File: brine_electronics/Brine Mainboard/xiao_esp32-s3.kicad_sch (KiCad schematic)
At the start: 3 parts, among them U1 XIAO-ESP32-S3-SMD

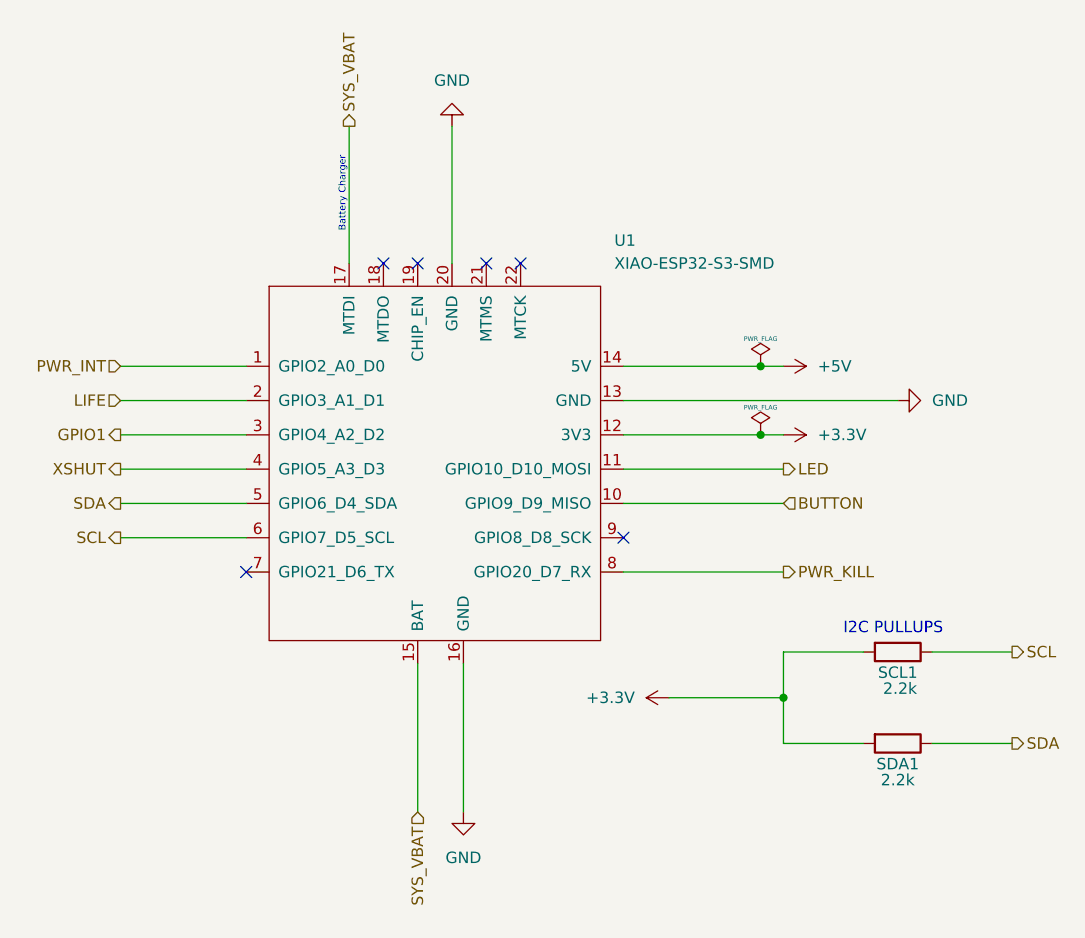
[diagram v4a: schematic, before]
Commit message: Updated GPIO button wiring ⚡
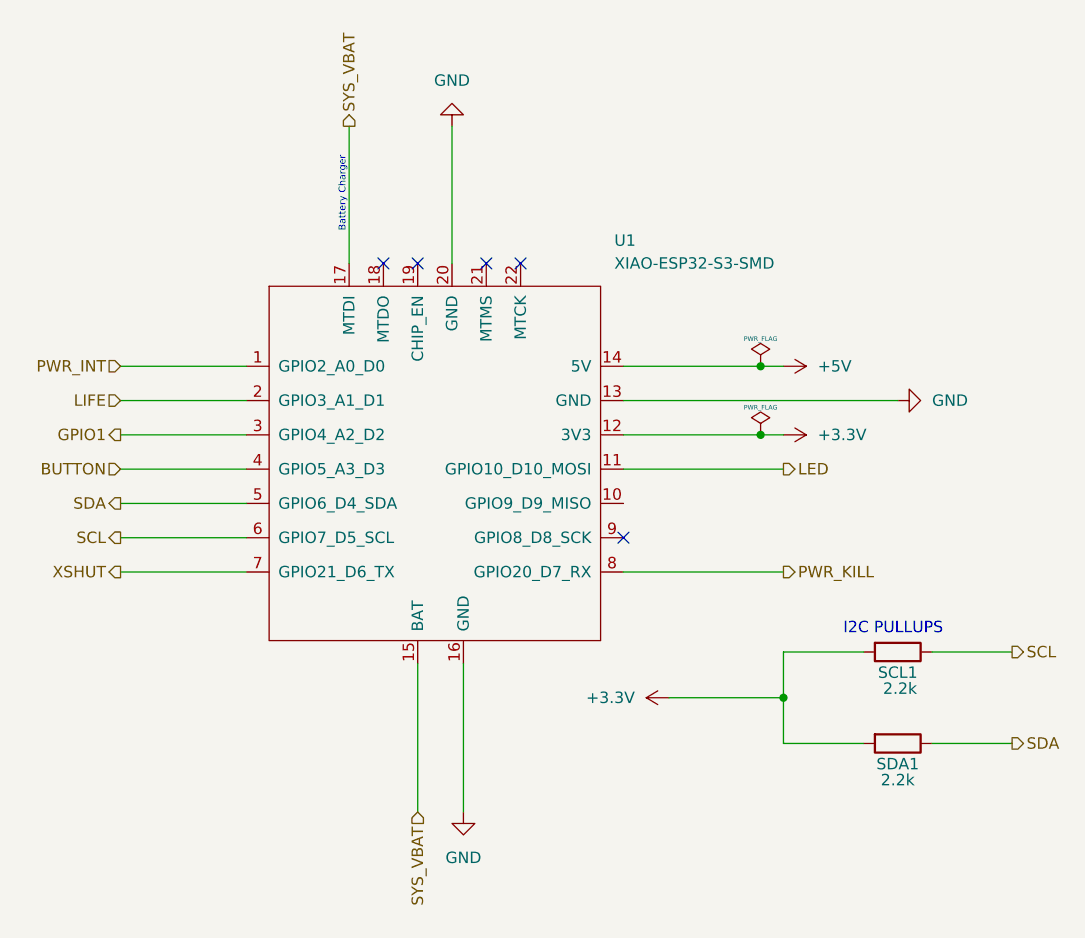
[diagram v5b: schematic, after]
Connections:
- net BUTTON: now also U1.4 (GPIO5_A3_D3); no longer U1.10 (GPIO9_D9_MISO)
- net XSHUT: now also U1.7 (GPIO21_D6_TX); no longer U1.4 (GPIO5_A3_D3)
- no-connect marks 6 -> 5
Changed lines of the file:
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@@
-	)
-	(no_connect
-		(at 118.11 113.03)
 	)
 	(no_connect
@@
 	(wire
 		(pts
+			(xy 175.26 90.17) (xy 177.8 90.17)
+		)
+		(stroke
+			(width 0)
+			(type default)
+		)
+	)
+	(wire
+		(pts
+			(xy 104.14 93.98) (xy 118.11 93.98)
+		)
+		(stroke
+			(width 0)
+			(type default)
+		)
+	)
+	(wire
+		(pts
+			(xy 104.14 113.03) (xy 118.11 113.03)
+		)
+		(stroke
+			(width 0)
+			(type default)
+		)
+	)
+	(wire
+		(pts
+			(xy 177.8 127) (xy 177.8 132.08)
+		)
+		(stroke
+			(width 0)
+			(type default)
+		)
+	)
+	(wire
+		(pts
+			(xy 137.16 123.19) (xy 137.16 139.7)
+		)
+		(stroke
+			(width 0)
+			(type default)
+		)
+	)
+	(wire
+		(pts
+			(xy 140.97 63.5) (xy 140.97 78.74)
+		)
+		(stroke
+			(width 0)
+			(type default)
+		)
+	)
+	(wire
+		(pts
+			(xy 104.14 105.41) (xy 118.11 105.41)
+		)
+		(stroke
+			(width 0)
+			(type default)
+		)
+	)
+	(wire
+		(pts
+			(xy 129.54 63.5) (xy 129.54 78.74)
+		)
+		(stroke
+			(width 0)
+			(type default)
+		)
+	)
+	(wire
+		(pts
+			(xy 175.26 97.79) (xy 177.8 97.79)
+		)
+		(stroke
+			(width 0)
+			(type default)
+		)
+	)
+	(wire
+		(pts
+			(xy 160.02 90.17) (xy 175.26 90.17)
+		)
+		(stroke
+			(width 0)
+			(type default)
+		)
+	)
+	(wire
+		(pts
+			(xy 104.14 90.17) (xy 118.11 90.17)
+		)
+		(stroke
+			(width 0)
+			(type default)
+		)
+	)
+	(wire
+		(pts
+			(xy 177.8 132.08) (xy 186.69 132.08)
+		)
+		(stroke
+			(width 0)
+			(type default)
+		)
+	)
+	(wire
+		(pts
+			(xy 160.02 97.79) (xy 175.26 97.79)
+		)
+		(stroke
+			(width 0)
+			(type default)
+		)
+	)
+	(wire
+		(pts
 			(xy 104.14 101.6) (xy 118.11 101.6)
-		)
-		(stroke
-			(width 0)
-			(type default)
-		)
-	)
-	(wire
-		(pts
-			(xy 175.26 90.17) (xy 177.8 90.17)
-		)
-		(stroke
-			(width 0)
-			(type default)
-		)
-	)
-	(wire
-		(pts
-			(xy 104.14 93.98) (xy 118.11 93.98)
-		)
-		(stroke
-			(width 0)
-			(type default)
-		)
-	)
-	(wire
-		(pts
-			(xy 177.8 127) (xy 177.8 132.08)
-		)
-		(stroke
-			(width 0)
-			(type default)
-		)
-	)
-	(wire
-		(pts
-			(xy 137.16 123.19) (xy 137.16 139.7)
-		)
-		(stroke
-			(width 0)
-			(type default)
-		)
-	)
-	(wire
-		(pts
-			(xy 140.97 63.5) (xy 140.97 78.74)
-		)
-		(stroke
-			(width 0)
-			(type default)
-		)
-	)
-	(wire
-		(pts
-			(xy 104.14 105.41) (xy 118.11 105.41)
-		)
-		(stroke
-			(width 0)
-			(type default)
-		)
-	)
-	(wire
-		(pts
-			(xy 129.54 63.5) (xy 129.54 78.74)
-		)
-		(stroke
-			(width 0)
-			(type default)
-		)
-	)
-	(wire
-		(pts
-			(xy 175.26 97.79) (xy 177.8 97.79)
-		)
-		(stroke
-			(width 0)
-			(type default)
-		)
-	)
-	(wire
-		(pts
-			(xy 160.02 90.17) (xy 175.26 90.17)
-		)
-		(stroke
-			(width 0)
-			(type default)
-		)
-	)
-	(wire
-		(pts
-			(xy 104.14 90.17) (xy 118.11 90.17)
-		)
-		(stroke
-			(width 0)
-			(type default)
-		)
-	)
-	(wire
-		(pts
-			(xy 177.8 132.08) (xy 186.69 132.08)
-		)
-		(stroke
-			(width 0)
-			(type default)
-		)
-	)
-	(wire
-		(pts
-			(xy 160.02 97.79) (xy 175.26 97.79)
-		)
-		(stroke
-			(width 0)
-			(type default)
-		)
-	)
-	(wire
-		(pts
-			(xy 160.02 105.41) (xy 177.8 105.41)
 		)
 		(stroke
@@
 	(hierarchical_label "XSHUT"
 		(shape output)
+		(at 104.14 113.03 180)
+		(effects
+			(font
+				(size 1.27 1.27)
+			)
+			(justify right)
+		)
+	)
+	(hierarchical_label "BUTTON"
+		(shape input)
 		(at 104.14 101.6 180)
 		(effects
@@
 		)
 	)
-	(hierarchical_label "BUTTON"
-		(shape input)
-		(at 177.8 105.41 0)
-		(effects
-			(font
-				(size 1.27 1.27)
-			)
-			(justify left)
-		)
-	)

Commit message: Updated production files 🏭
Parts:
- SCL1, SDA1: LCSC Part # (none) -> C17520
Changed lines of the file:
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@@
+			)
+		)
+		(property "Color" ""
+			(at 190.5 132.08 90)
+			(hide yes)
+			(show_name no)
+			(do_not_autoplace no)
+			(effects
+				(font
+					(size 1.27 1.27)
+				)
+			)
+		)
+		(property "LCSC Part #" "C17520"
+			(at 190.5 132.08 90)
+			(hide yes)
+			(show_name no)
+			(do_not_autoplace no)
+			(effects
+				(font
+					(size 1.27 1.27)
+				)
 			)
 		)
@@
 			)
 		)
+		(property "Color" ""
+			(at 139.7 101.6 0)
+			(hide yes)
+			(show_name no)
+			(do_not_autoplace no)
+			(effects
+				(font
+					(size 1.27 1.27)
+				)
+			)
+		)
+		(property "LCSC Part #" ""
+			(at 139.7 101.6 0)
+			(hide yes)
+			(show_name no)
+			(do_not_autoplace no)
+			(effects
+				(font
+					(size 1.27 1.27)
+				)
+			)
+		)
 		(pin "1"
 		)
@@
 			(hide yes)
 			(show_name no)
+			(do_not_autoplace no)
+			(effects
+				(font
+					(size 1.27 1.27)
+				)
+			)
+		)
+		(property "Color" ""
+			(at 190.5 121.92 90)
+			(hide yes)
+			(show_name no)
+			(do_not_autoplace no)
+			(effects
+				(font
+					(size 1.27 1.27)
+				)
+			)
+		)
+		(property "LCSC Part #" "C17520"
+			(at 190.5 121.92 90)
+			(hide yes)
+			(show_name no)

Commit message: Updated electronics production files 🏭
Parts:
- SCL1, SDA1: JLCPCB Part # (none) -> C17520; LCSC Part # C17520 -> (none)
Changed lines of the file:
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@@
 			)
 		)
-		(property "LCSC Part #" "C17520"
+		(property "JLCPCB Part #" "C17520"
 			(at 190.5 132.08 90)
 			(hide yes)
@@
 			)
 		)
-		(property "LCSC Part #" ""
-			(at 139.7 101.6 0)
-			(hide yes)
-			(show_name no)
-			(do_not_autoplace no)
-			(effects
-				(font
-					(size 1.27 1.27)
-				)
-			)
-		)
 		(pin "1"
 		)
@@
 			)
 		)
-		(property "LCSC Part #" "C17520"
+		(property "JLCPCB Part #" "C17520"
 			(at 190.5 121.92 90)
 			(hide yes)
